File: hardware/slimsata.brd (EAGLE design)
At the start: 20.3 x 54.6 mm, 2 parts, among them CON1 MOLEX_67492

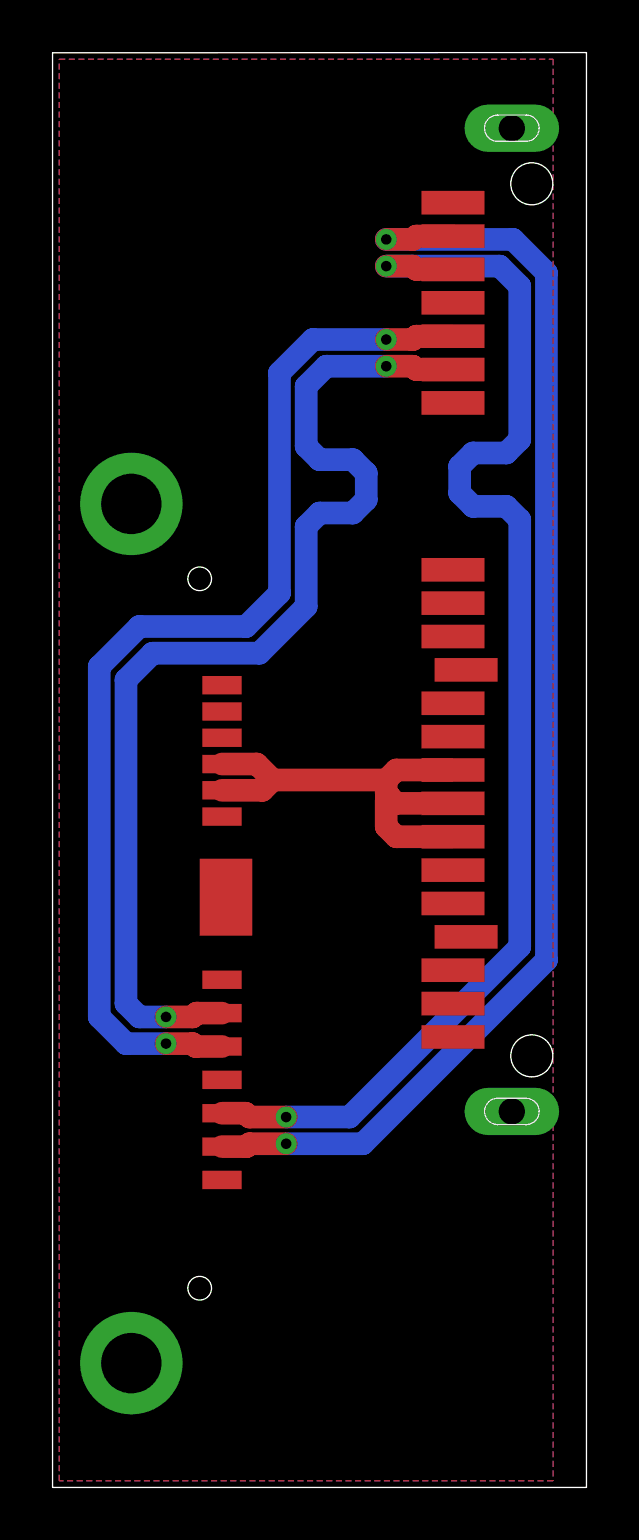
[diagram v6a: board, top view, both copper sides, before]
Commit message: Abstände Datenleitungen <-> GND auf 20 mil vergrössert.
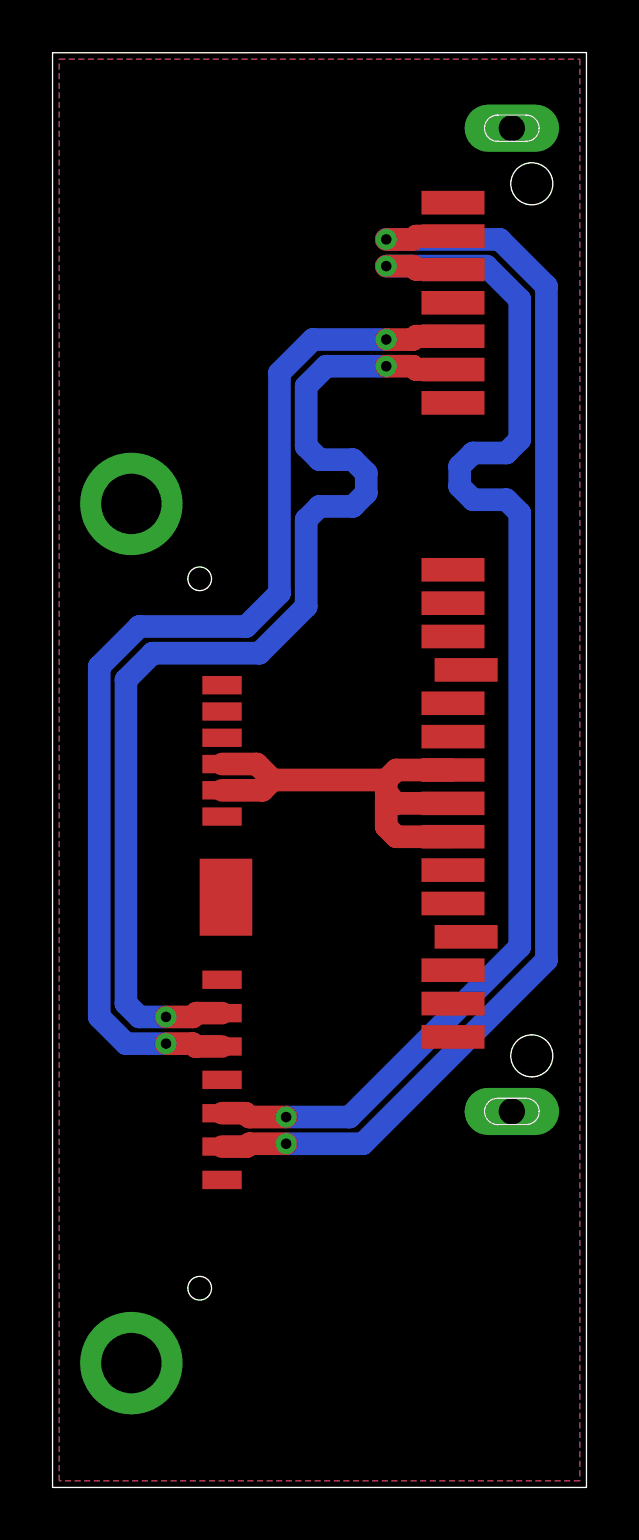
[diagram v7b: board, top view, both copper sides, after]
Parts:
- CON2: value (none) -> MOLEX_47300
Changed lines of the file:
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@@
 <class number="0" name="default" width="0" drill="0">
+</class>
+<class number="1" name="data" width="0" drill="0">
+</class>
+<class number="2" name="gnd" width="0" drill="0">
+<clearance class="1" value="0.508"/>
 </class>
 </classes>
@@
 <elements>
 <element name="CON1" library="sata" package="MOLEX_67492" value="MOLEX_67492" x="20.32" y="33.02" rot="R90"/>
-<element name="CON2" library="sata" package="MOLEX_47300-1005" value="" x="0" y="21.082" rot="R270"/>
+<element name="CON2" library="sata" package="MOLEX_47300-1005" value="MOLEX_47300" x="0" y="21.082" rot="R270"/>
 </elements>
 <signals>
-<signal name="N$5">
+<signal name="N$5" class="1">
 <contactref element="CON1" pad="S2"/>
 <contactref element="CON2" pad="S2"/>
@@
 <wire x1="13.716" y1="47.498" x2="12.7" y2="47.498" width="0.8636" layer="1"/>
 <via x="12.7" y="47.498" extent="1-16" drill="0.4"/>
-<wire x1="12.7" y1="47.498" x2="17.526" y2="47.498" width="0.8636" layer="16"/>
-<wire x1="17.526" y1="47.498" x2="18.796" y2="46.228" width="0.8636" layer="16"/>
-<wire x1="18.796" y1="20.066" x2="18.796" y2="46.228" width="0.8636" layer="16"/>
+<wire x1="12.7" y1="47.498" x2="17.018" y2="47.498" width="0.8636" layer="16"/>
+<wire x1="17.018" y1="47.498" x2="18.796" y2="45.72" width="0.8636" layer="16"/>
+<wire x1="18.796" y1="20.066" x2="18.796" y2="45.72" width="0.8636" layer="16"/>
 <wire x1="18.796" y1="20.066" x2="11.811" y2="13.081" width="0.8636" layer="16"/>
 <wire x1="11.811" y1="13.081" x2="8.89" y2="13.081" width="0.8636" layer="16"/>
@@
 <wire x1="7.493" y1="13.081" x2="8.89" y2="13.081" width="0.8636" layer="1"/>
 </signal>
-<signal name="N$6">
+<signal name="N$6" class="1">
 <contactref element="CON1" pad="S3"/>
 <contactref element="CON2" pad="S3"/>
@@
 <wire x1="13.716" y1="46.482" x2="12.7" y2="46.482" width="0.8636" layer="1"/>
 <via x="12.7" y="46.482" extent="1-16" drill="0.4"/>
-<wire x1="12.7" y1="46.482" x2="17.018" y2="46.482" width="0.8636" layer="16"/>
-<wire x1="17.018" y1="46.482" x2="17.78" y2="45.72" width="0.8636" layer="16"/>
-<wire x1="17.78" y1="45.72" x2="17.78" y2="39.878" width="0.8636" layer="16"/>
+<wire x1="12.7" y1="46.482" x2="16.51" y2="46.482" width="0.8636" layer="16"/>
+<wire x1="16.51" y1="46.482" x2="17.78" y2="45.212" width="0.8636" layer="16"/>
+<wire x1="17.78" y1="45.212" x2="17.78" y2="39.878" width="0.8636" layer="16"/>
 <wire x1="17.78" y1="39.878" x2="17.272" y2="39.37" width="0.8636" layer="16"/>
 <wire x1="17.272" y1="39.37" x2="16.002" y2="39.37" width="0.8636" layer="16"/>
 <wire x1="16.002" y1="39.37" x2="15.494" y2="38.862" width="0.8636" layer="16"/>
-<wire x1="15.494" y1="38.862" x2="15.494" y2="37.846" width="0.8636" layer="16"/>
-<wire x1="15.494" y1="37.846" x2="16.002" y2="37.338" width="0.8636" layer="16"/>
-<wire x1="16.002" y1="37.338" x2="17.272" y2="37.338" width="0.8636" layer="16"/>
-<wire x1="17.272" y1="37.338" x2="17.78" y2="36.83" width="0.8636" layer="16"/>
-<wire x1="17.78" y1="36.83" x2="17.78" y2="20.574" width="0.8636" layer="16"/>
+<wire x1="15.494" y1="38.862" x2="15.494" y2="38.1" width="0.8636" layer="16"/>
+<wire x1="15.494" y1="38.1" x2="16.002" y2="37.592" width="0.8636" layer="16"/>
+<wire x1="16.002" y1="37.592" x2="17.272" y2="37.592" width="0.8636" layer="16"/>
+<wire x1="17.272" y1="37.592" x2="17.78" y2="37.084" width="0.8636" layer="16"/>
+<wire x1="17.78" y1="37.084" x2="17.78" y2="20.574" width="0.8636" layer="16"/>
 <wire x1="17.78" y1="20.574" x2="11.303" y2="14.097" width="0.8636" layer="16"/>
 <wire x1="11.303" y1="14.097" x2="8.89" y2="14.097" width="0.8636" layer="16"/>
@@
 <wire x1="7.493" y1="14.097" x2="8.89" y2="14.097" width="0.8636" layer="1"/>
 </signal>
-<signal name="N$7">
+<signal name="N$7" class="1">
 <contactref element="CON1" pad="S5"/>
 <contactref element="CON2" pad="S5"/>
@@
 <wire x1="5.334" y1="16.891" x2="4.318" y2="16.891" width="0.8636" layer="1"/>
 </signal>
-<signal name="N$8">
+<signal name="N$8" class="1">
 <contactref element="CON1" pad="S6"/>
 <contactref element="CON2" pad="S6"/>
@@
 <wire x1="10.16" y1="39.116" x2="11.43" y2="39.116" width="0.8636" layer="16"/>
 <wire x1="11.43" y1="39.116" x2="11.938" y2="38.608" width="0.8636" layer="16"/>
-<wire x1="11.938" y1="37.592" x2="11.938" y2="38.608" width="0.8636" layer="16"/>
-<wire x1="11.938" y1="37.592" x2="11.43" y2="37.084" width="0.8636" layer="16"/>
-<wire x1="11.43" y1="37.084" x2="10.16" y2="37.084" width="0.8636" layer="16"/>
-<wire x1="10.16" y1="37.084" x2="9.652" y2="36.576" width="0.8636" layer="16"/>
-<wire x1="9.652" y1="36.576" x2="9.652" y2="33.528" width="0.8636" layer="16"/>
+<wire x1="11.938" y1="37.846" x2="11.938" y2="38.608" width="0.8636" layer="16"/>
+<wire x1="11.938" y1="37.846" x2="11.43" y2="37.338" width="0.8636" layer="16"/>
+<wire x1="11.43" y1="37.338" x2="10.16" y2="37.338" width="0.8636" layer="16"/>
+<wire x1="10.16" y1="37.338" x2="9.652" y2="36.83" width="0.8636" layer="16"/>
+<wire x1="9.652" y1="36.83" x2="9.652" y2="33.528" width="0.8636" layer="16"/>
 <wire x1="9.652" y1="33.528" x2="7.874" y2="31.75" width="0.8636" layer="16"/>
 <wire x1="7.874" y1="31.75" x2="3.81" y2="31.75" width="0.8636" layer="16"/>
@@
 <wire x1="12.7" y1="26.162" x2="12.827" y2="26.289" width="0.8636" layer="1"/>
 </signal>
-<signal name="GND">
+<signal name="GND" class="2">
 <contactref element="CON2" pad="S1"/>
 <contactref element="CON1" pad="S1"/>
@@
 <polygon width="0.4064" layer="1">
 <vertex x="0.254" y="54.356"/>
-<vertex x="19.05" y="54.356"/>
-<vertex x="19.05" y="0.254"/>
+<vertex x="20.066" y="54.356"/>
+<vertex x="20.066" y="0.254"/>
 <vertex x="0.254" y="0.254"/>
 </polygon>
 <polygon width="0.4064" layer="16">
 <vertex x="0.254" y="54.356"/>
-<vertex x="19.05" y="54.356"/>
-<vertex x="19.05" y="0.254"/>
+<vertex x="20.066" y="54.356"/>
+<vertex x="20.066" y="0.254"/>
 <vertex x="0.254" y="0.254"/>
 </polygon>
 </signal>
 </signals>
+<errors>
+</errors>
 </board>
 </drawing>
